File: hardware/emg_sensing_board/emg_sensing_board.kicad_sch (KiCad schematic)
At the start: 53 parts, among them J1 USB_A_0480370001, J2 Conn_01x09, J3 DEBUG, U1 W25Q128JV, U2 RP2040, U3 RN4871-I/RM140, U4 MCP1702T-3302E_CB, U5 MCP6021, Y1 12MHz

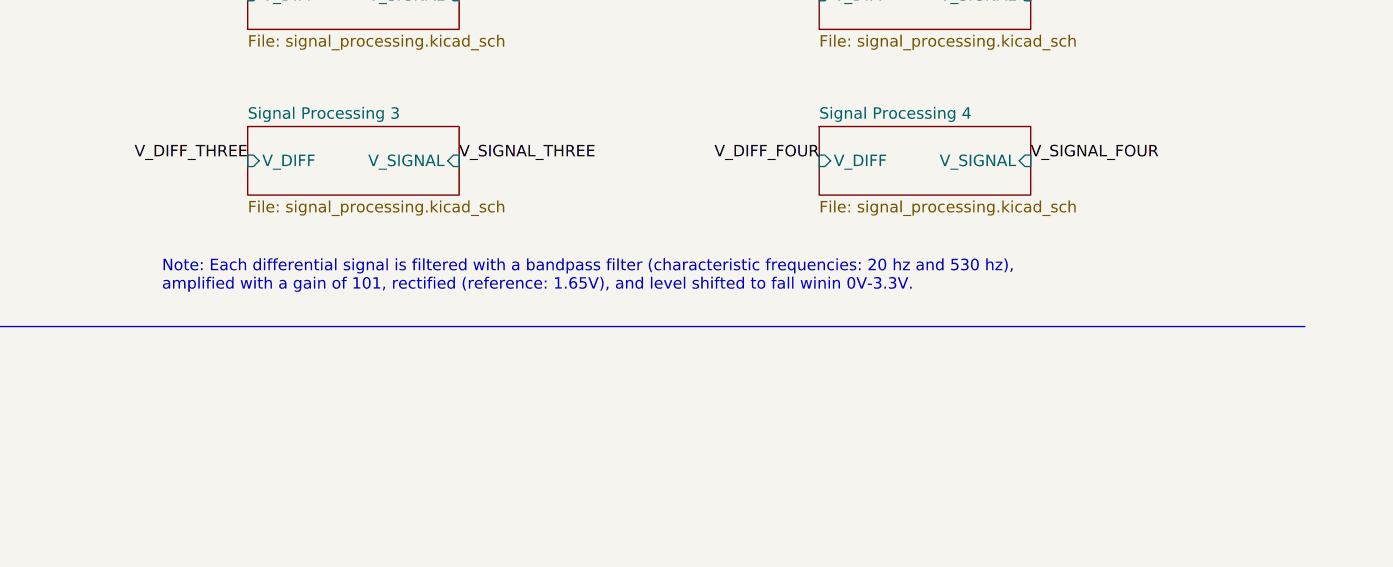
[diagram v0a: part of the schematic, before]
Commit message: updated gain
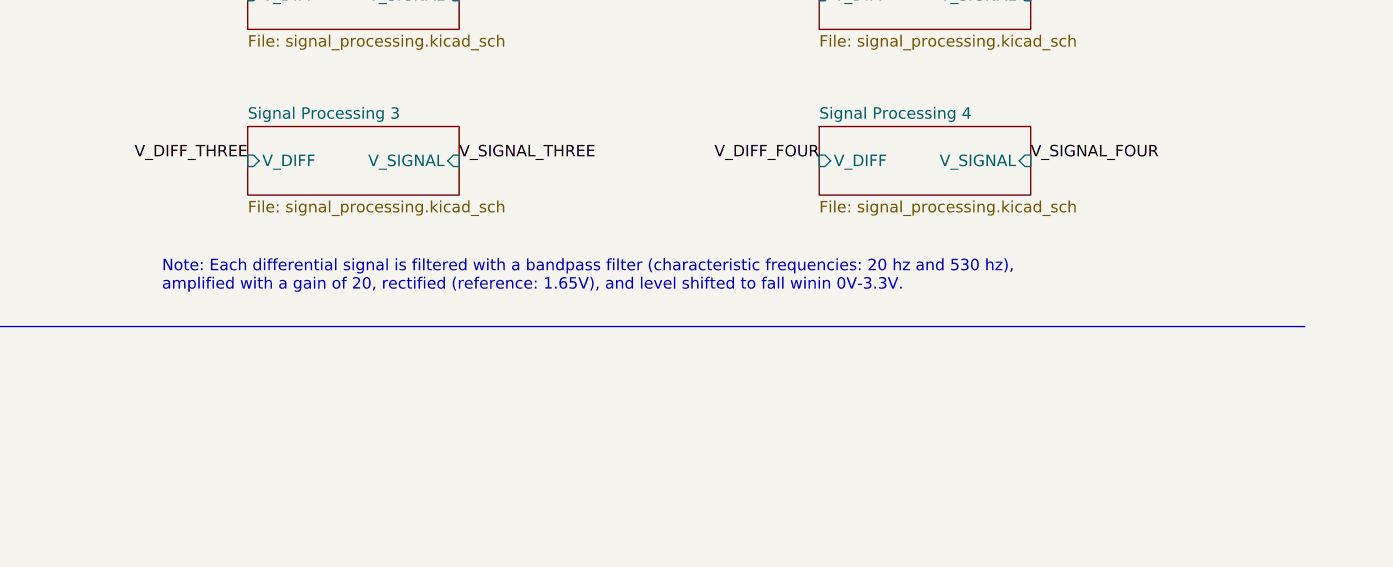
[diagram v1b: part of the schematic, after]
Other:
- note added: "Note: Each differential signal is filtered with a bandpass filter (characteristic frequencies: 20 hz and 530 hz), amplified with a gain of 20, rectified (reference: 1.65V), and level shifted to fall winin 0V-3.3V."
- note removed: "Note: Each differential signal is filtered with a bandpass filter (characteristic frequencies: 20 hz and 530 hz), amplified with a gain of 101, rectified (reference: 1.65V), and level shifted to fall winin 0V-3.3V."
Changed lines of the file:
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@@
     (effects (font (size 2.54 2.54)) (justify left bottom))
   )
-  (text "Note: Each differential signal is filtered with a bandpass filter (characteristic frequencies: 20 hz and 530 hz),\namplified with a gain of 101, rectified (reference: 1.65V), and level shifted to fall winin 0V-3.3V.\n"
+  (text "Note: Each differential signal is filtered with a bandpass filter (characteristic frequencies: 20 hz and 530 hz),\namplified with a gain of 20, rectified (reference: 1.65V), and level shifted to fall winin 0V-3.3V.\n"
     (at 281.305 119.38 0)
     (effects (font (size 1.27 1.27)) (justify left bottom))
